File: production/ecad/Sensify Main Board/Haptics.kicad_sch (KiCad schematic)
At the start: 17 parts, among them J10 Conn_01x02_Socket, J4 Conn_01x02_Socket, J8 Conn_01x02_Socket, J9 Conn_01x02_Socket, U1 DRV2605LDGSR, U2 DRV2605LDGSR, U3 DRV2605LDGSR, U4 DRV2605LDGSR

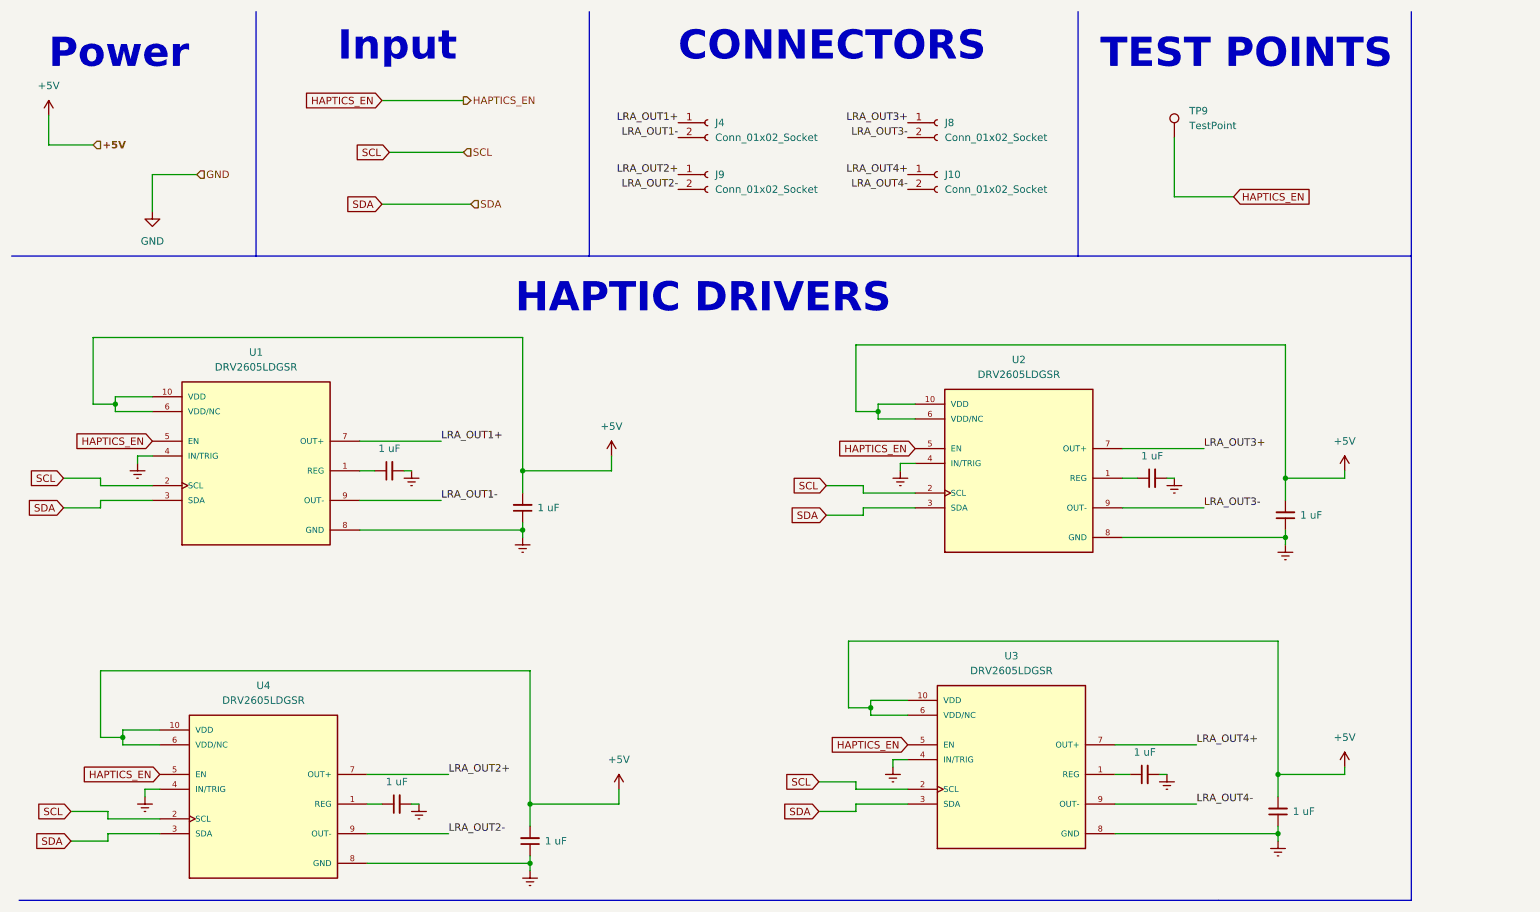
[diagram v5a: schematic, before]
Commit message: Added Test Point footprints, fixed Haptics footprints, fixed IMU footprints
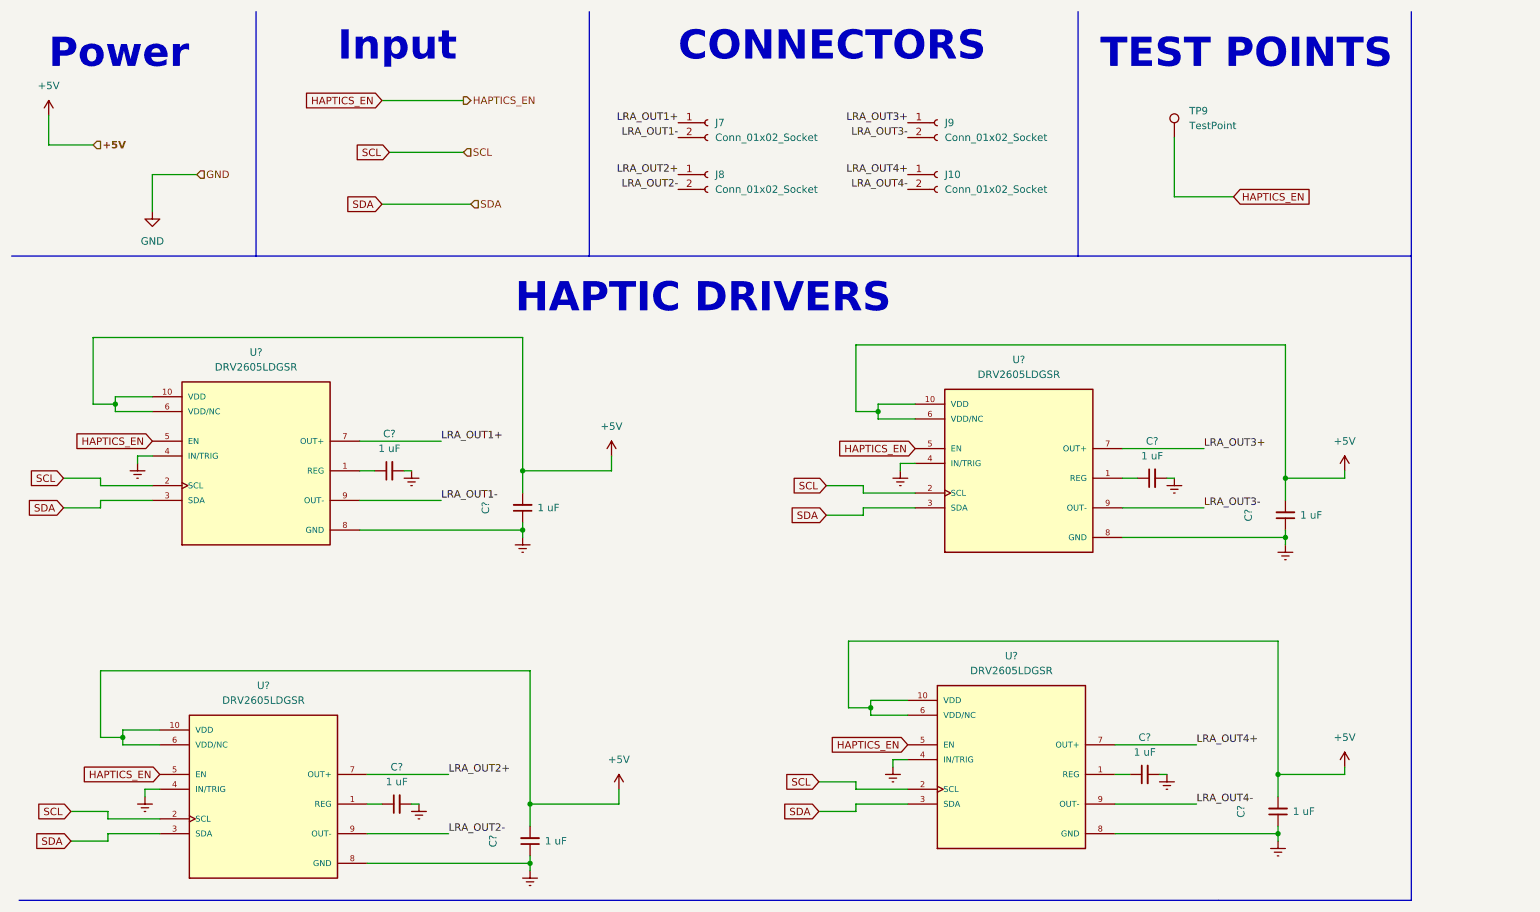
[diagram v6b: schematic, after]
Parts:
- C?: renamed from C3; footprint Resistor_SMD:R_0402_1005Metric -> Capacitor_SMD:C_0402_1005Metric
- C?: renamed from C4; footprint (none) -> Capacitor_SMD:C_0402_1005Metric
- C?: renamed from C6; footprint (none) -> Capacitor_SMD:C_0402_1005Metric
- C?: renamed from C15; footprint Resistor_SMD:R_0402_1005Metric -> Capacitor_SMD:C_0402_1005Metric
- C?: renamed from C1; footprint Resistor_SMD:R_0402_1005Metric -> Capacitor_SMD:C_0402_1005Metric
- C?: renamed from C5; footprint Resistor_SMD:R_0402_1005Metric -> Capacitor_SMD:C_0402_1005Metric
- C?: renamed from C16; footprint (none) -> Capacitor_SMD:C_0402_1005Metric
- C?: renamed from C2; footprint (none) -> Capacitor_SMD:C_0402_1005Metric
- TP9: footprint (none) -> TestPoint:TestPoint_Pad_D2.0mm
- renumbered J4 to J7, J9 to J8, J8 to J9, U1 to U?, U2 to U?, U4 to U?, U3 to U?

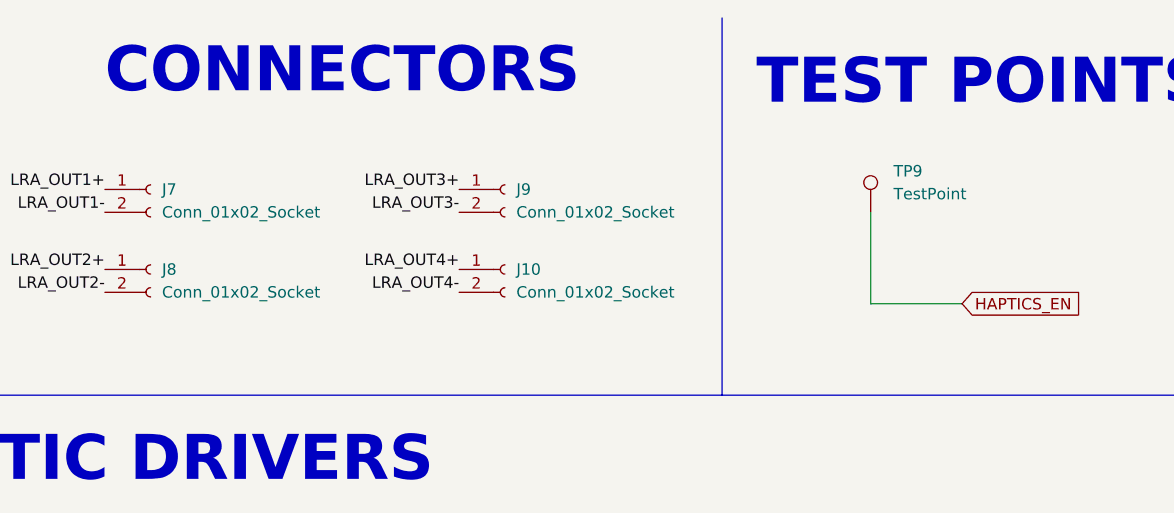
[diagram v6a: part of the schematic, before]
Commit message: Added Labels to Test Points
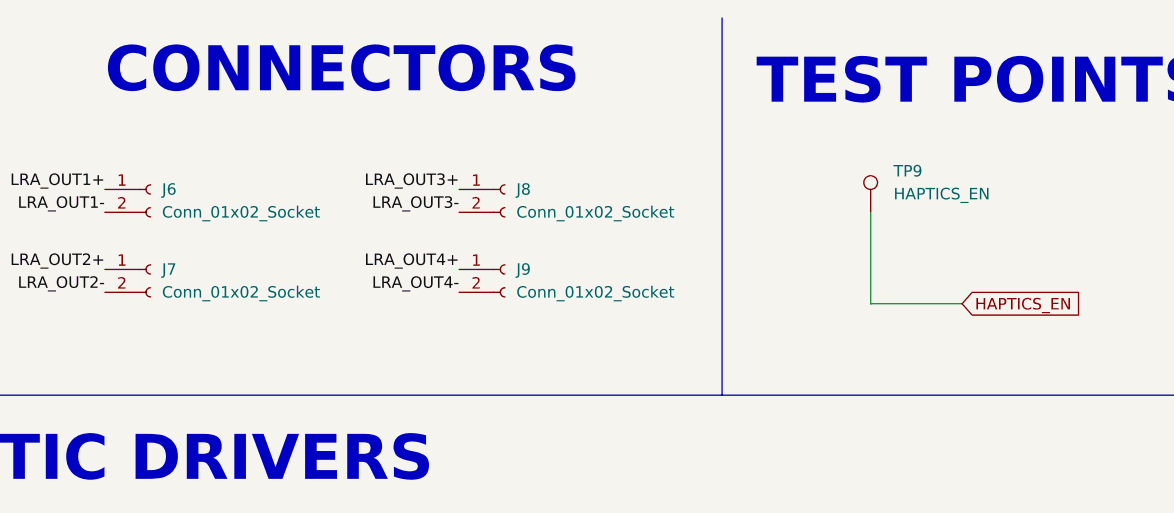
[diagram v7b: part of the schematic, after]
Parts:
- TP9: value TestPoint -> HAPTICS_EN
- renumbered J7 to J6, J8 to J7, J9 to J8, J10 to J9
